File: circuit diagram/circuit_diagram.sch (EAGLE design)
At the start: 12 parts, among them M1 MOTOR, U1 MD22

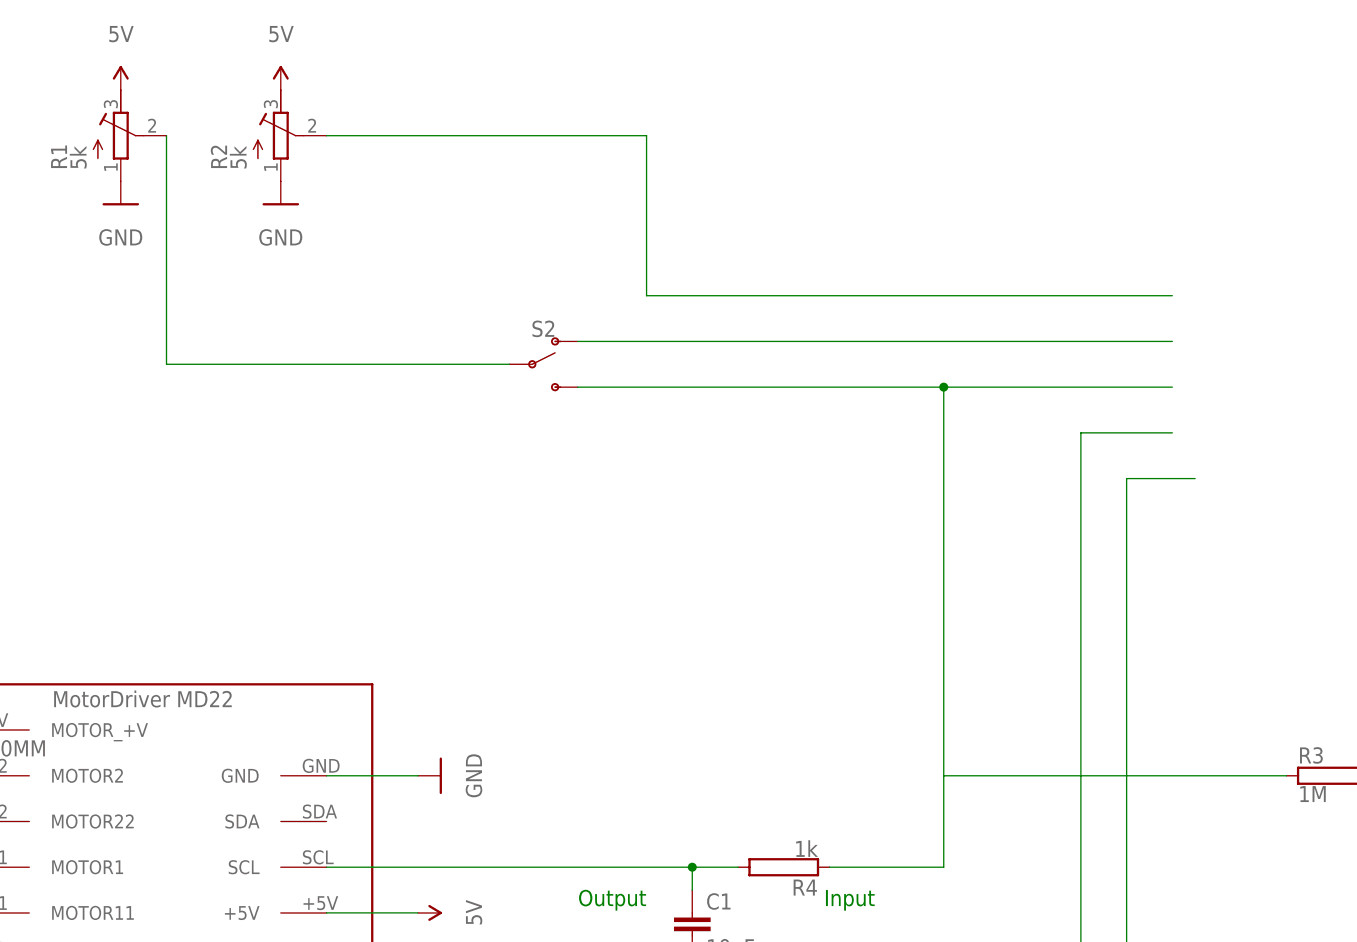
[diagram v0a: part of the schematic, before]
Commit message: New Circuit Diagram and new Gears
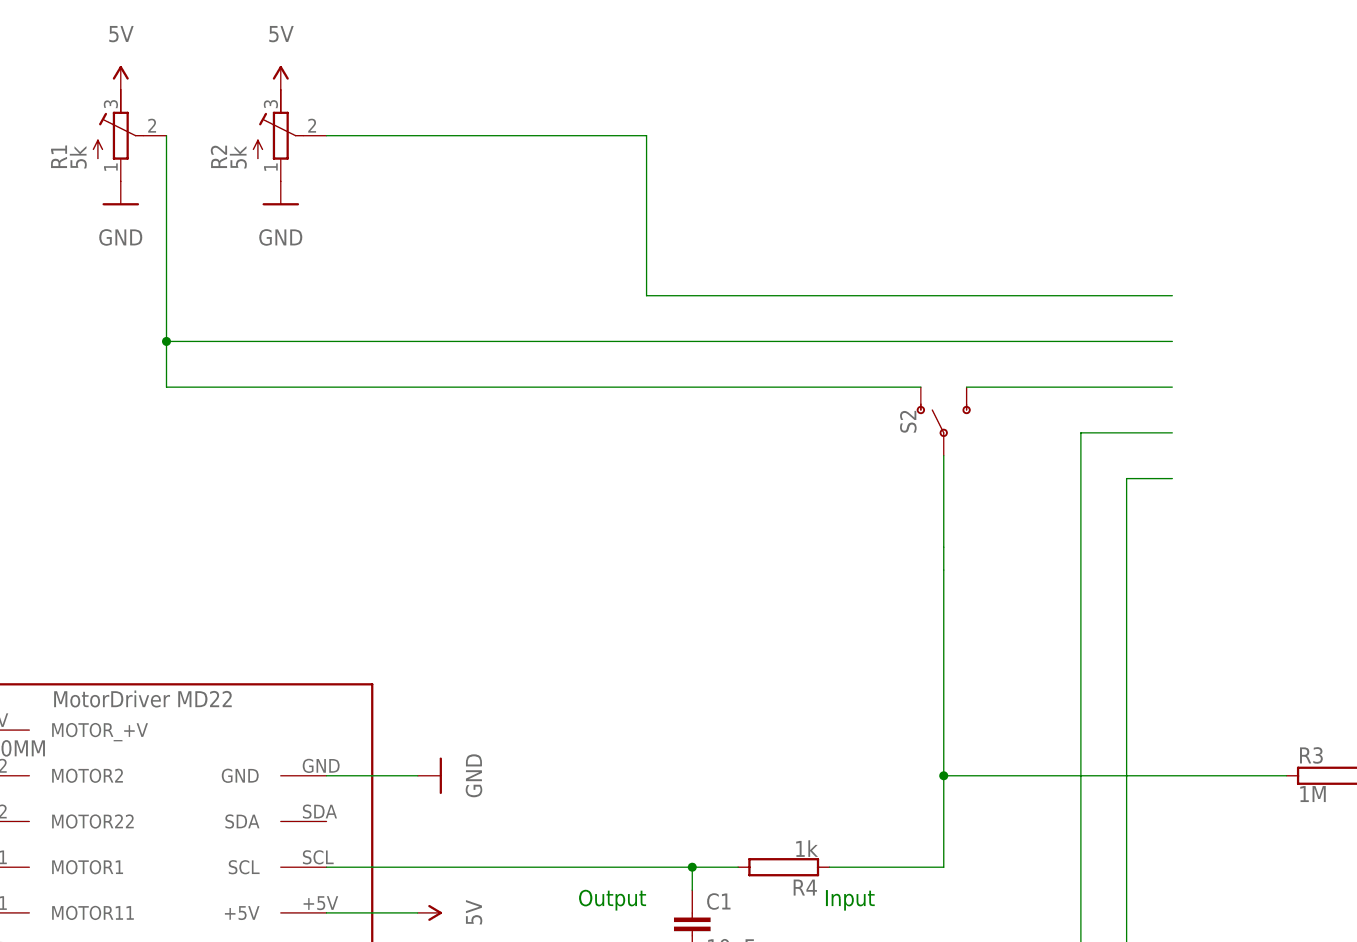
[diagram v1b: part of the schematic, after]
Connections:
- removed net N$8: S2.O
- new net N$12: R3.1, R4.1, S2.P
- net N$4: no longer R3.1, R4.1
- net N$6: now also S2.O; no longer S2.P
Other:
- moved on the sheet: S2
